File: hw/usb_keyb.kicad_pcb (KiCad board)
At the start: 4 copper layers, 99.1 x 48.3 mm, 103 parts, among them J10 SPI, J11 RMII, J12 PS2, J2 Micro_SD_Card, J3 USB_1, J4 ZX-BUS, J5 MX_ROW, J6 MX_COL, J7 I2C, J8 UART, J9 PROG, SW1 RESET, SW2 OUTPUT, SW3 MATRIX, U1 LM3671MF, U2 STM32F407VETx, U3 STMPS2161STR, U4 NUP4201MR6, U5 74LS245, Y1 8MHz

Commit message: Обновлена плата
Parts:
- removed C25: NFM21PC104R1E3D, Projects:NFM21P
- removed J5: MX_ROW, Socket_Strips:Socket_Strip_Straight_1x12_Pitch2.54mm
- removed J6: MX_COL, Socket_Strips:Socket_Strip_Straight_1x12_Pitch2.54mm
- removed JP1: 5Vin, Pin_Headers:Pin_Header_Straight_1x02_Pitch2.54mm
- added D1: L1, LEDs:LED_0805, F.Cu at (176.5, 90.2)
- added D2: L2, LEDs:LED_0805, F.Cu at (174.6, 90.2)
- added D3: ERR, LEDs:LED_0805, F.Cu at (172.7, 90.2)
- added J13: OUT_JMP, Pin_Headers:Pin_Header_Straight_1x03_Pitch2.54mm, F.Cu at (111.8, 97.2)
- added J14: MTX_JMP, Pin_Headers:Pin_Header_Straight_1x08_Pitch2.54mm, F.Cu at (109.2, 85.7)
- added R11: 10k, Resistors_SMD:R_0805, B.Cu at (189.2, 93.9)
- added R13: 10k, Resistors_SMD:R_0805, B.Cu at (170.7, 94.0)
- added R62: 10k, Resistors_SMD:R_0805, F.Cu at (170.7, 94.0)
- C11: moved to B.Cu
- C16, C6, C7, C8: moved to F.Cu
- moved C11 42.9 mm to (107.3, 102.9), turned to 90 degrees
- moved R18 35.1 mm to (128.9, 93.3), turned to 270 degrees
- moved C7 33.2 mm to (146.8, 87.4), turned to 0 degrees
- moved R19 31.5 mm to (126.4, 93.3), turned to 270 degrees
- moved C10 29.7 mm to (122.6, 93.8), turned to 180 degrees
- moved J10 28.4 mm to (134.0, 99.7)
- moved R12 24.8 mm to (167.1, 94.0)
- moved J7 24.3 mm to (128.9, 96.5)
- moved C6 24.0 mm to (143.3, 95.0), turned to 90 degrees
- moved C8 18.5 mm to (122.6, 102.6), turned to 180 degrees
- moved C16 13.1 mm to (178.1, 84.6), turned to 270 degrees
- moved J12 13.1 mm to (134.0, 102.9)
- moved R10 5.22 mm to (188.3, 91.3), turned to 270 degrees
- moved U3 4.27 mm to (189.2, 96.9), turned to 90 degrees
- moved C17 3.81 mm to (188.7, 101.9), turned to 90 degrees
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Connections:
- R12 pad 1: +3V3 -> LED_1
- R12 pad 2: Net-(R10-Pad2) -> Net-(D1-Pad2)
- U2 pad 35: LED_1 -> OUT0
- U2 pad 36: LED_2 -> OUT1
- U2 pad 37: LED_3 -> OUT2
- U2 pad 67: OUT0 -> LED_1
- U2 pad 68: OUT1 -> LED_2
- U2 pad 69: OUT2 -> LED_3
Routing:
- net TXD1: track 0.00 -> 83.3 mm, vias 0 -> 1
- net TX_EN: track 0.00 -> 80.2 mm, vias 0 -> 1
- net TXD0: track 0.00 -> 79.2 mm, vias 0 -> 1
- net RXD1: track 0.00 -> 72.1 mm
- net CRS: track 0.00 -> 67.2 mm
- net RXD0: track 0.00 -> 67.0 mm
- net +5V: track 0.00 -> 58.7 mm, vias 0 -> 2
- net MDIO: track 0.00 -> 55.1 mm, vias 0 -> 2
- net ECK: track 0.00 -> 54.3 mm
- net MDC: track 0.00 -> 52.0 mm
- net OUT2: track 8.73 -> 56.3 mm
- net OUT1: track 6.12 -> 53.0 mm
- net MTX1: track 0.00 -> 44.7 mm, vias 0 -> 1
- net +3V3: track 24.7 -> 68.1 mm, vias 1 -> 6
- net OUT0: track 7.36 -> 48.9 mm
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
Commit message: Обновлена разводка питания на внутренних слоях, для DRC
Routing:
- net GND: track 106.2 -> 367.3 mm, vias 42 -> 55
- net +3V3: track 68.1 -> 273.7 mm, vias 6 -> 25
- net Net-(C17-Pad1): track 15.1 -> 27.4 mm
- net SDA: track 0.00 -> 2.22 mm
- net SCL: track 0.00 -> 2.22 mm
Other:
- net class Default: clearance 0.175 -> 0.165
- rule trace_clearance: 0.175 -> 0.165
- rule trace_min: 0.175 -> 0.165

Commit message: Обновлена плата
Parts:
- C12: moved to B.Cu
- moved R1 10.1 mm to (182.5, 78.0), turned to 270 degrees
- moved U5 9.85 mm to (157.5, 82.3)
- moved C2 8.68 mm to (168.3, 79.5)
- moved L1 8.60 mm to (174.0, 78.6)
- moved U1 8.38 mm to (178.9, 78.0)
- moved C12 3.79 mm to (184.9, 75.9), turned to 90 degrees
- moved C7 2.40 mm to (144.8, 88.7), turned to 90 degrees
- moved J4 2.03 mm to (140.3, 67.7)
- moved R20 2.03 mm to (139.1, 72.7)
- moved R21 2.03 mm to (136.5, 72.7)
- moved R22 2.03 mm to (134.0, 72.7)
- moved R23 2.03 mm to (141.6, 72.7)
- moved R24 2.03 mm to (121.3, 72.7)
- moved R25 2.03 mm to (149.2, 72.7)
- moved R26 2.03 mm to (146.7, 72.7)
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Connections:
- R20 pad 1: +3V3 -> +5V
- R21 pad 1: +3V3 -> +5V
- R22 pad 1: +3V3 -> +5V
- R23 pad 1: +3V3 -> +5V
- R24 pad 1: +3V3 -> +5V
- R25 pad 1: +3V3 -> +5V
- R26 pad 1: +3V3 -> +5V
- R27 pad 1: +3V3 -> +5V
- R28 pad 1: +3V3 -> +5V
- R29 pad 1: +3V3 -> +5V
- R30 pad 1: +3V3 -> +5V
- R31 pad 1: +3V3 -> +5V
- R32 pad 1: +3V3 -> +5V
- R33 pad 1: +3V3 -> +5V
- R34 pad 1: +3V3 -> +5V
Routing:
- net +5V: track 58.7 -> 251.6 mm, vias 2 -> 18
- net RES: track 1.43 -> 102.9 mm, vias 1 -> 3
- net ZA11: track 1.57 -> 83.4 mm, vias 0 -> 2
- net ZM1n: track 1.57 -> 79.4 mm, vias 0 -> 1
- net ZA12: track 1.57 -> 79.3 mm, vias 0 -> 4
- net ZA9: track 1.57 -> 79.0 mm, vias 0 -> 3
- net ZA13: track 1.57 -> 78.7 mm, vias 0 -> 4
- net ZA10: track 1.57 -> 78.5 mm, vias 0 -> 3
- net ZA14: track 1.57 -> 77.5 mm, vias 0 -> 3
- net ZA15: track 1.57 -> 75.9 mm, vias 0 -> 3
- net ZA8: track 1.57 -> 73.3 mm, vias 0 -> 1
- net ZA7: track 1.57 -> 58.3 mm, vias 0 -> 2
- net USB_PWR: track 0.00 -> 45.3 mm, vias 0 -> 3
- net MTX7: track 4.72 -> 49.1 mm, vias 0 -> 2
- net MTX6: track 4.72 -> 47.2 mm, vias 0 -> 2
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
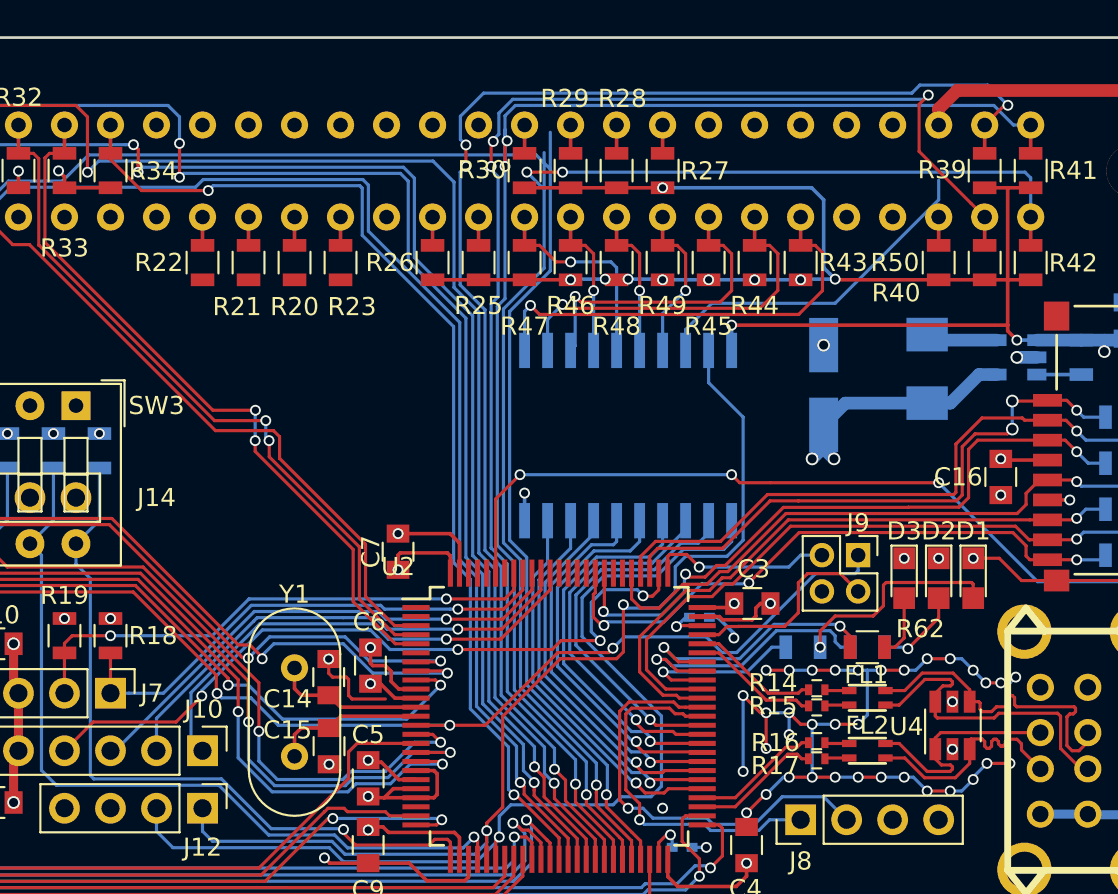
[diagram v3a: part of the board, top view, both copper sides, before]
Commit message: Завершена черновая трассировка платы
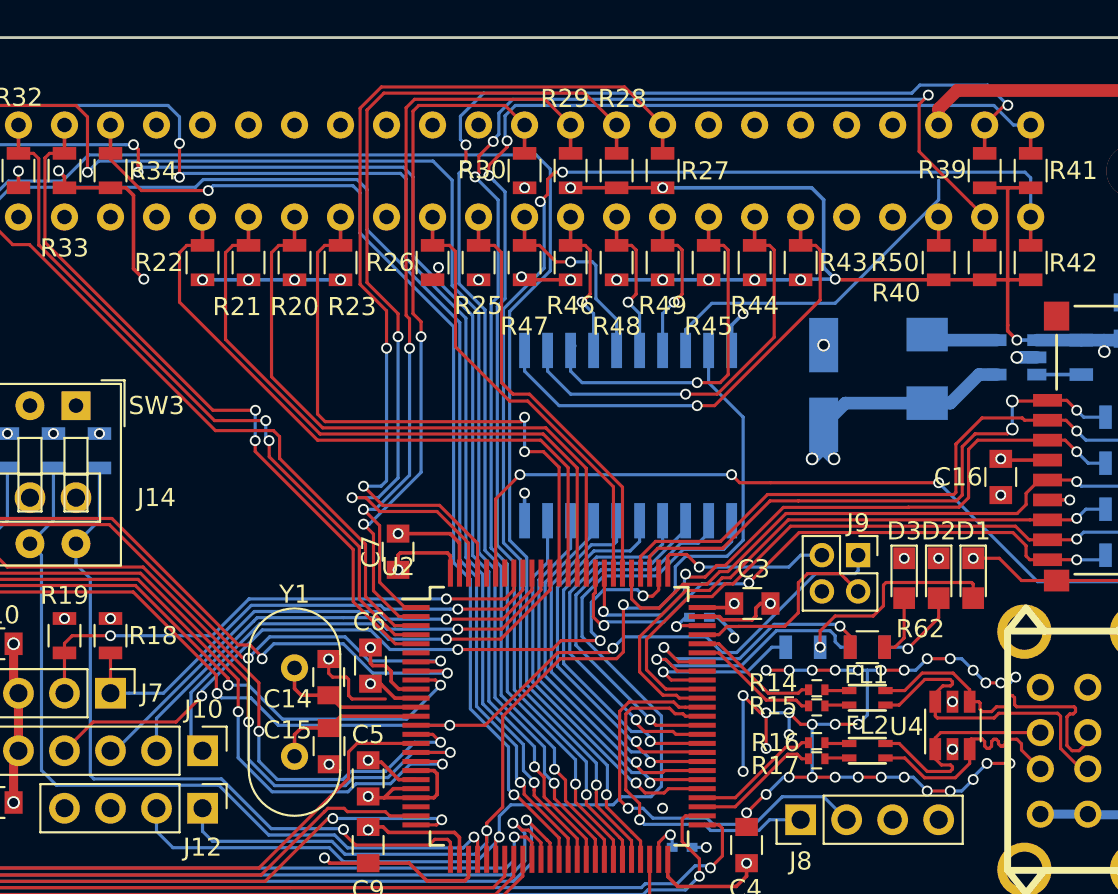
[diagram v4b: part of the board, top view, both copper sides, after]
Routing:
- net ZA0: track 1.57 -> 51.4 mm, vias 0 -> 2
- net ZA1: track 1.57 -> 49.6 mm, vias 0 -> 2
- net ZA2: track 1.57 -> 42.1 mm, vias 0 -> 2
- net ZA3: track 1.57 -> 39.6 mm, vias 0 -> 2
- net ZWRn: track 1.57 -> 36.8 mm
- net ZRDn: track 1.57 -> 36.0 mm
- net ZIORQn: track 1.57 -> 35.1 mm
- net ZMREQn: track 1.57 -> 33.7 mm, vias 0 -> 2
- net ZNMIn: track 1.57 -> 24.9 mm
- net ZINTn: track 1.57 -> 24.0 mm
- net +5V: track 251.6 -> 269.4 mm, vias 18 -> 27
- net ZA15: track 75.9 -> 72.4 mm
- net ZD2: track 17.2 -> 20.3 mm
- net ZD1: track 20.4 -> 23.1 mm
- net ZM1n: track 79.4 -> 77.4 mm
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
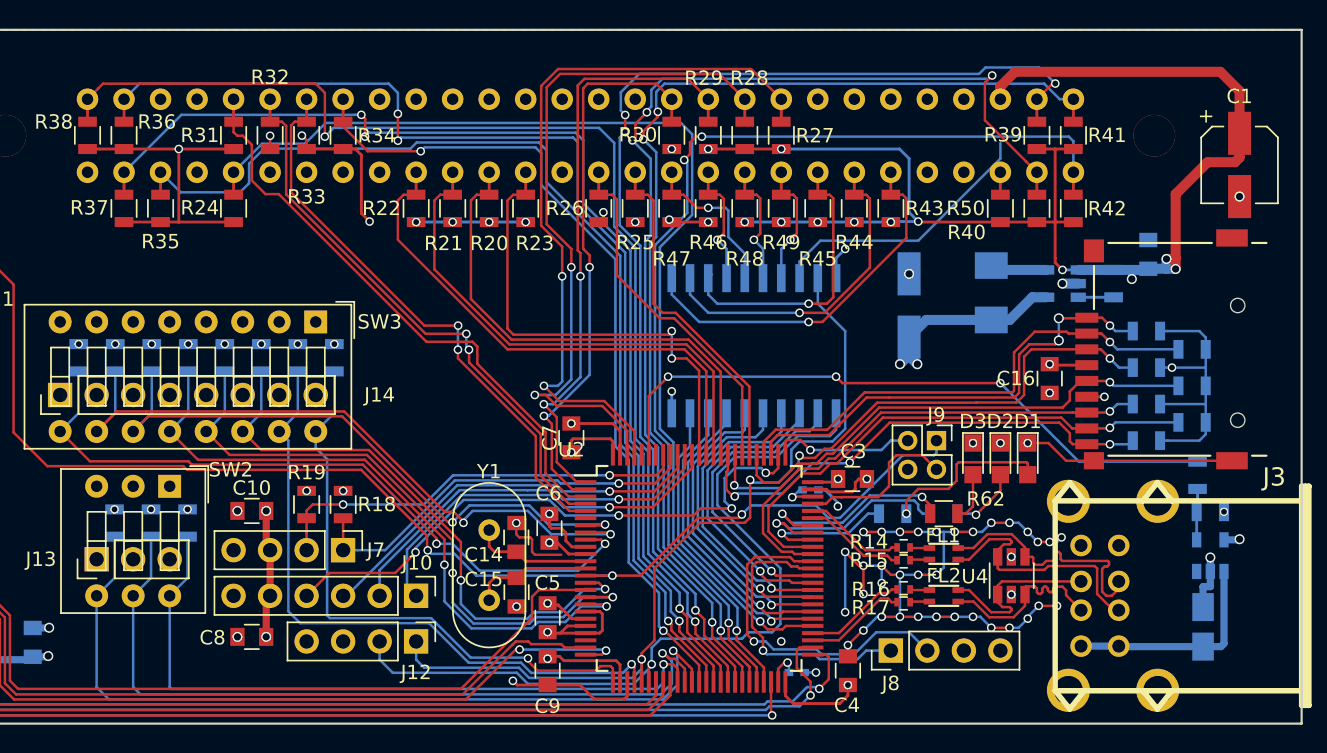
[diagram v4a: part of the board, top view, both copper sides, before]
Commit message: Обновлена трассировка платы
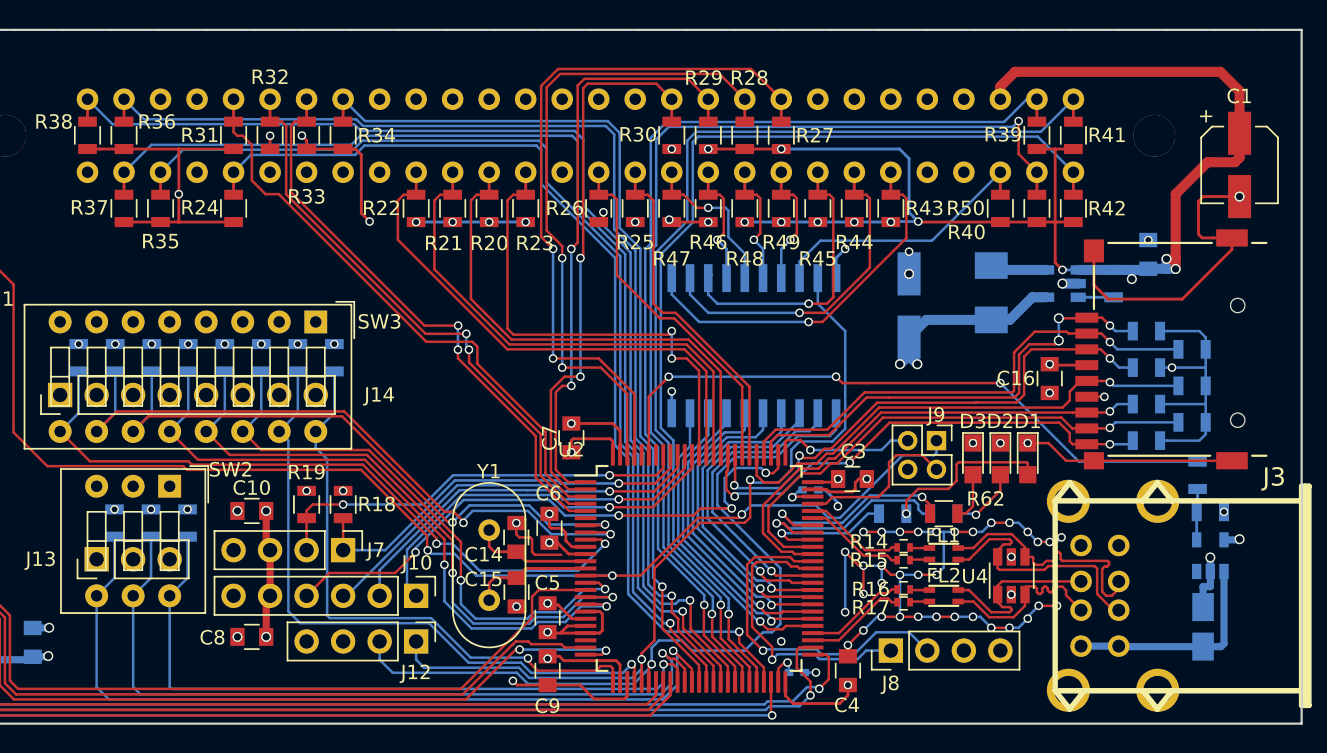
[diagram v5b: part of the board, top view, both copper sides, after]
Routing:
- net GND: track 357.8 -> 506.3 mm, vias 60 -> 62
- net +3V3: track 251.0 -> 311.1 mm
- net ZA12: track 79.3 -> 70.2 mm, vias 4 -> 1
- net ZA13: track 79.5 -> 72.0 mm, vias 4 -> 2
- net +5V: track 269.4 -> 276.8 mm
- net ZM1n: track 77.4 -> 70.3 mm
- net ZA14: track 76.3 -> 70.9 mm, vias 3 -> 1
- net ZA7: track 58.1 -> 62.3 mm, vias 2 -> 1
- net ZA1: track 49.6 -> 45.9 mm
- net ZA11: track 83.4 -> 80.6 mm, vias 2 -> 1
- net ZA15: track 72.4 -> 70.5 mm, vias 3 -> 1
- net ZA0: track 51.4 -> 49.8 mm
- net ZA10: track 78.5 -> 76.9 mm, vias 3 -> 1
- net ZA8: track 73.1 -> 71.5 mm
- net ZD7: track 20.7 -> 19.3 mm
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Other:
- rule trace_min: 0.165 -> 0.16
